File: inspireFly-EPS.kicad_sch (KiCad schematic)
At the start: 76 parts, among them J1 USB4085-GF-A_REVB, J2 Conn_01x02_Pin, Q10 SQJA62EP-T1_GE3, Q3 SQJA62EP-T1_GE3, Q4 SQJA62EP-T1_GE3, Q5 SQJA62EP-T1_GE3, Q6 SQJA62EP-T1_GE3, Q7 SQJA62EP-T1_GE3, Q8 SQJA62EP-T1_GE3, Q9 SQJA62EP-T1_GE3, U1 STM32U575RIT6, U2 BQ25750RRVR, U3 TCAN332DCNR, U5 INA180A3IDBVT, U6 INA180A3IDBVT, U7 INA180A3IDBVT

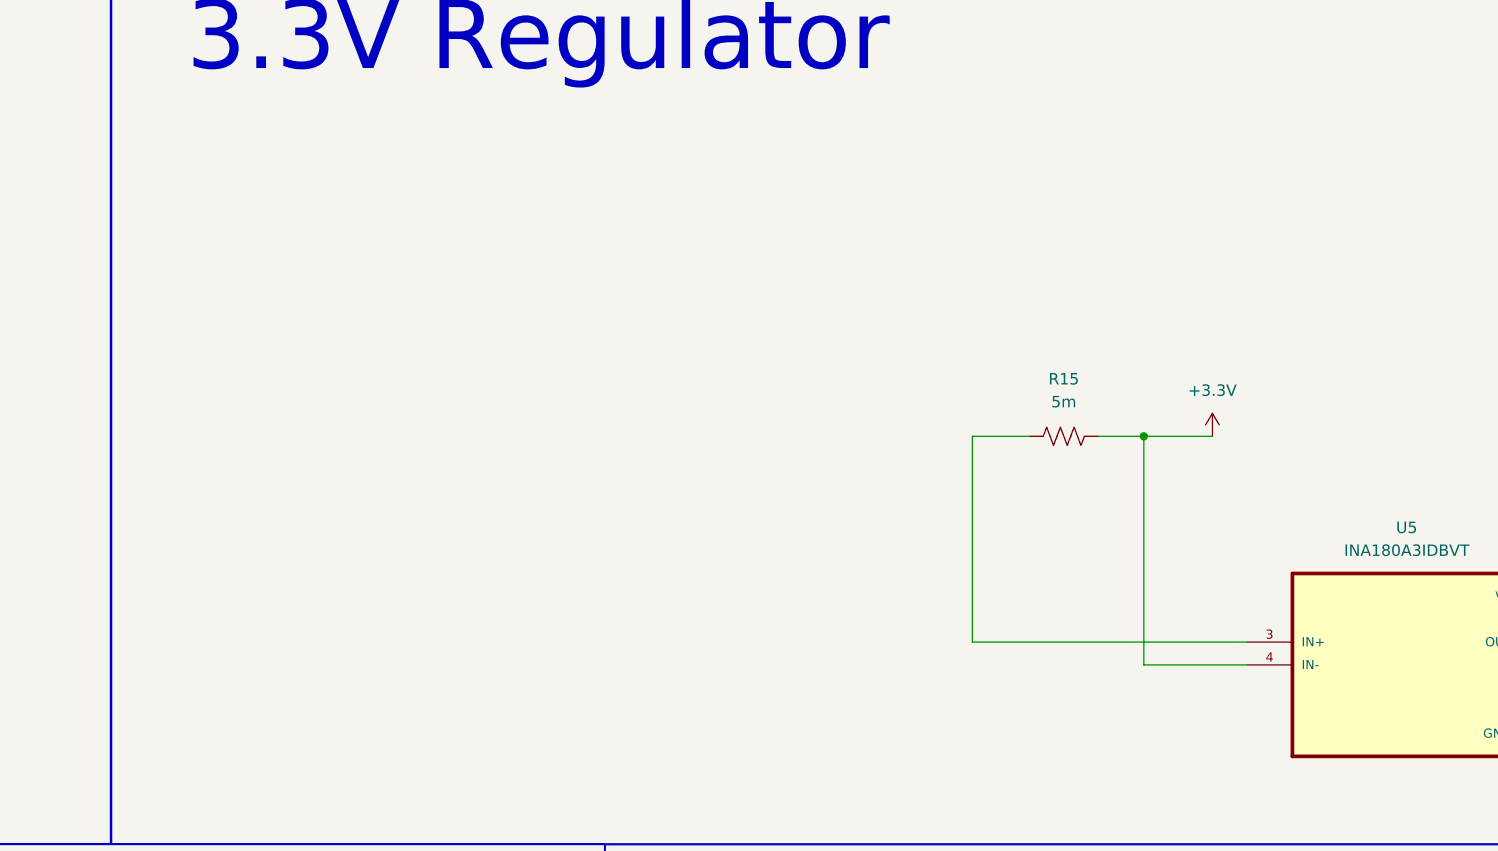
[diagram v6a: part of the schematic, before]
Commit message: added 3.3V to schematic
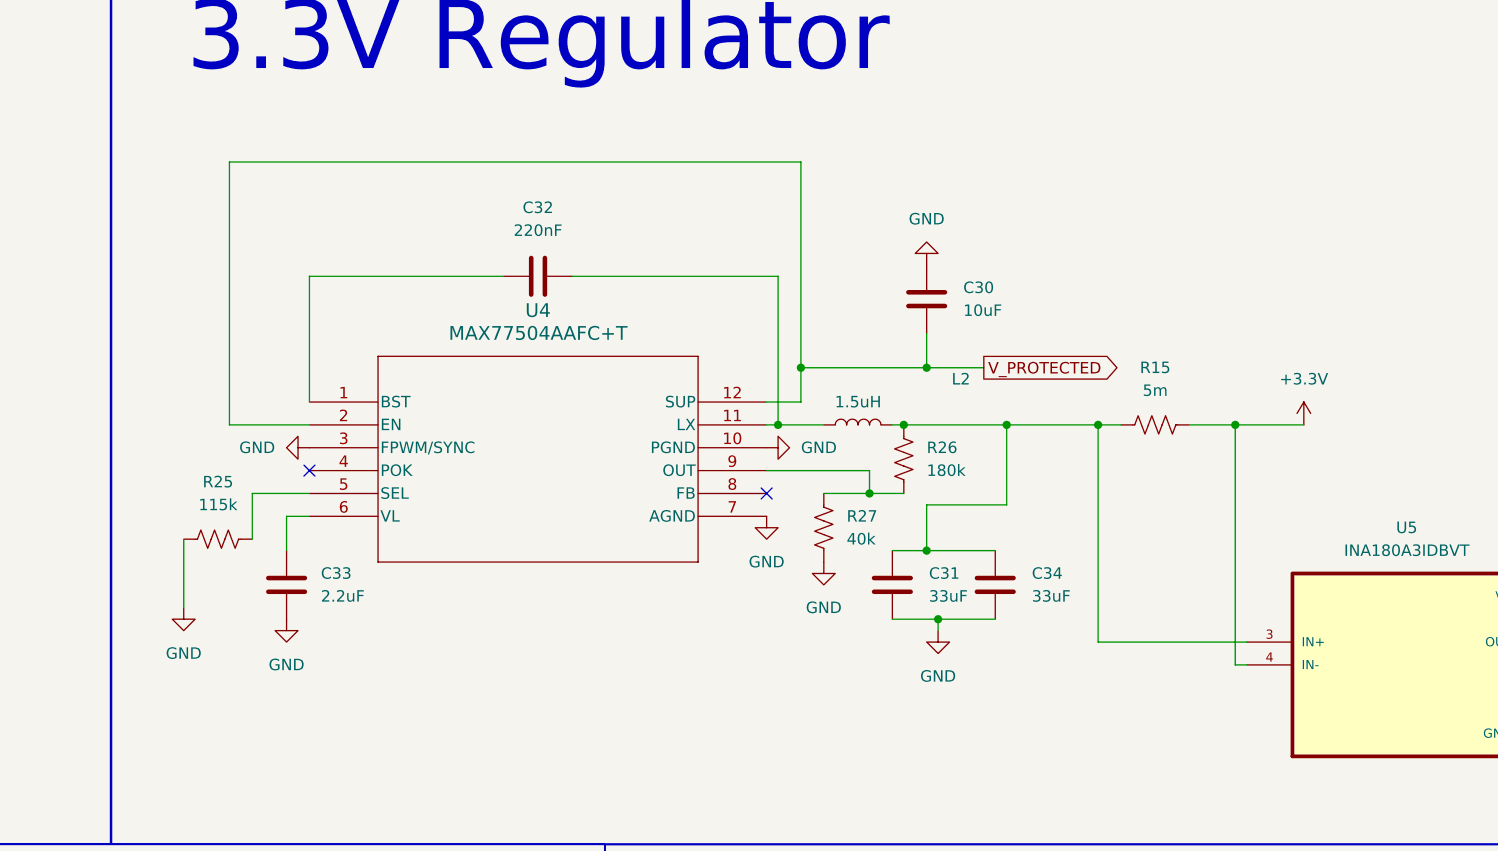
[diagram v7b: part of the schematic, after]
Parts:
- added C30: 10uF, symbol Device:C
- added C31, C34: 33uF, symbol Device:C
- added C32: 220nF, symbol Device:C
- added C33: 2.2uF, symbol Device:C
- added L2: 1.5uH, symbol Device:L
- added R25: 115k, symbol Device:R_US
- added R26: 180k, symbol Device:R_US
- added R27: 40k, symbol Device:R_US
- added U4: MAX77504AAFC+T, 21-100406_F122A2F+2_MXM, symbol InspireFly-EPS-sym_lib:MAX77504AAFC+T
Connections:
- net GND: now also C30.2, C31.1, C33.1, C34.1, R25.1, R27.1, U4.10 (PGND), U4.3 (FPWM/SYNC), U4.7 (AGND)
- net V_PROTECTED: now also C30.1, U4.12 (SUP), U4.2 (EN)
- net at R15.1, U5.3 (IN+): now also C31.2, C34.2, L2.2, R26.2
- new net: C32.1, L2.1, U4.11 (LX)
- new net: C33.2, U4.6 (VL)
- new net: C32.2, U4.1 (BST)
- new net: R26.1, R27.2, U4.9 (OUT)
- new net: R25.2, U4.5 (SEL)
- no-connect marks 9 -> 11
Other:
- moved on the sheet: R15

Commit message: Schematic additions, some routing changes
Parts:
- added C37, C38: 10uF, symbol Device:C
- added C39: 100nF, Capacitor_SMD:C_0805_2012Metric_Pad1.18x1.45mm_HandSolder, symbol Device:C
- added C40, C41, C42, C43: 22uF, symbol Device:C
- added L3: 1.5uH, inspireFly-EPS-footprints:WE-MAPI_4020, symbol Device:L
- added R28: 40k, symbol Device:R_US
- added R29: 210k, symbol Device:R_US
- added U8, U9: TPS63070RNMR, inspireFly-EPS-footprints:VREG_TPS63070RNMR, symbol InspireFly-EPS-sym_lib:TPS63070RNMR
- C13: footprint Capacitor_SMD:C_0402_1005Metric_Pad0.74x0.62mm_HandSolder -> Capacitor_SMD:C_1206_3216Metric_Pad1.33x1.80mm_HandSolder
- C31, C34: value 33uF -> 22uF
- L2: footprint (none) -> inspireFly-EPS-footprints:WE-MAPI_4020
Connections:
- net GND: now also C37.2, C38.2, C39.2, C40.1, C41.1, C42.1, C43.1, R28.2, U8.10 (PGND), U8.15 (VSEL), U8.4 (GND), U8.6 (FB2)
- net V_PROTECTED: now also C37.1, U8.1 (PS/SYNC), U8.12_13 (VIN), U8.14 (EN)
- net at C31.2, C34.2, L2.2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: now also C40.2
- net at R16.1, U6.3 (IN+): now also C38.1, C41.2, C42.2, C43.2, R29.1, U8.7_8 (VOUT)
- new net: R28.1, R29.2, U8.5 (FB)
- new net: C39.1, U8.3 (VAUX)
- new net: L3.1, U8.11 (L1)
- new net: L3.2, U8.9 (L2)
- no-connect marks 11 -> 12
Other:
- moved on the sheet: C13, C31, C34, R27
